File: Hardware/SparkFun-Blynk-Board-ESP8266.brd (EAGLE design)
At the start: 50 x 41.9 mm, 104 parts, among them IC1 LMV358, Q1 2.5A/30V, Q2 MMBT2222A, Q3 MMBT2222A, U1 MCP73831, U2 ESP8266, U3 AP2112K-3.3V, U4 FT231XS-U, U5 W25Q32FVSS, U6 SI7021, Y1 26MHz

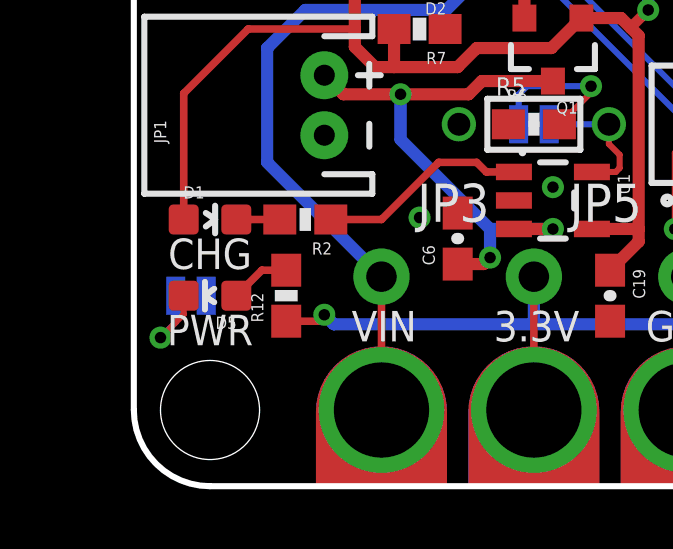
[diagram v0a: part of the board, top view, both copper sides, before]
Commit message: Moving PWR led a bit away from screwhead.
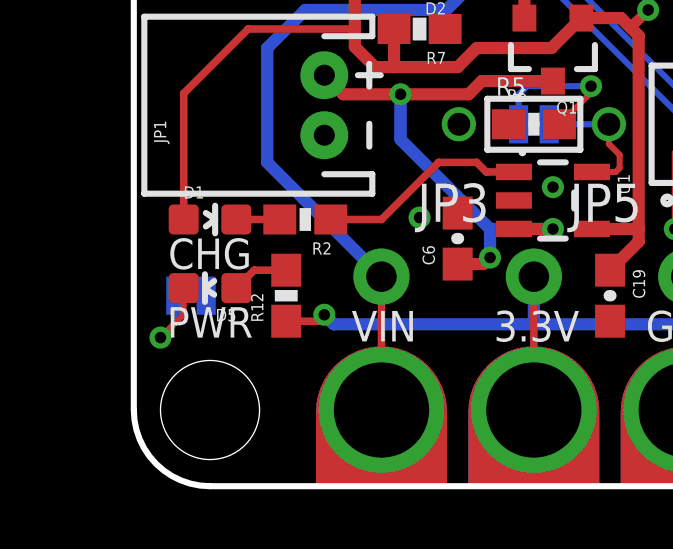
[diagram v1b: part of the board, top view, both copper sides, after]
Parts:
- moved D5 0.25 mm to (2.54, 6.60)
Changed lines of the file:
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@@
 <board>
 <plain>
-<text x="2.54" y="5.715" size="1.016" layer="21" font="vector" ratio="15" rot="R180" align="bottom-center">PWR</text>
+<text x="2.54" y="5.969" size="1.016" layer="21" font="vector" ratio="15" rot="R180" align="bottom-center">PWR</text>
 <wire x1="0" y1="2.54" x2="0" y2="39.37" width="0.2032" layer="20"/>
 <wire x1="0" y1="39.37" x2="2.54" y2="41.91" width="0.2032" layer="20" curve="-90"/>
@@
 <attribute name="PROD_ID" value="RES-07856" x="6.35" y="-36.83" size="1.778" layer="27" font="vector" ratio="15" rot="R90" display="off"/>
 </element>
-<element name="D5" library="SparkFun-LED" package="LED-0603" value="RED" x="2.54" y="6.35" rot="R90">
-<attribute name="PROD_ID" value="DIO-00819" x="8.89" y="-34.29" size="1.778" layer="27" font="vector" ratio="15" rot="R90" display="off"/>
+<element name="D5" library="SparkFun-LED" package="LED-0603" value="RED" x="2.54" y="6.604" rot="R90">
+<attribute name="PROD_ID" value="DIO-00819" x="8.89" y="-34.036" size="1.778" layer="27" font="vector" ratio="15" rot="R90" display="off"/>
 </element>
 <element name="R6" library="SparkFun-Resistors" package="0603-RES" value="2.0k" x="13.335" y="12.065">
@@
 <contactref element="D5" pad="C"/>
 <contactref element="SJ2" pad="2"/>
-<wire x1="1.663" y1="6.35" x2="1.663" y2="5.727" width="0.2032" layer="1"/>
+<wire x1="1.663" y1="6.604" x2="1.663" y2="5.727" width="0.2032" layer="1"/>
 <wire x1="1.663" y1="5.727" x2="0.889" y2="4.953" width="0.2032" layer="1"/>
 <via x="0.889" y="4.953" extent="1-16" drill="0.381"/>
@@
 <contactref element="D5" pad="A"/>
 <contactref element="R12" pad="2"/>
-<wire x1="3.417" y1="6.35" x2="4.267" y2="7.2" width="0.254" layer="1"/>
-<wire x1="4.267" y1="7.2" x2="5.08" y2="7.2" width="0.254" layer="1"/>
+<wire x1="3.417" y1="6.604" x2="4.013" y2="7.2" width="0.254" layer="1"/>
+<wire x1="4.013" y1="7.2" x2="5.08" y2="7.2" width="0.254" layer="1"/>
 </signal>
 <signal name="N$11">

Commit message: Adding values to all parts
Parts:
- JP1: value LiPo -> JST-2
- JP10, JP11, JP12, JP13, JP16, JP17, JP18, JP19, JP2, JP20, JP21, JP22, JP23, JP24, JP25, JP26, JP27, JP28, JP3, JP30, JP4, JP5, JP6, JP7, JP8, JP9, SJ1, SJ4: value (none) -> DNP
- JP14: value (none) -> JST-3
- JP15: value (none) -> USB
- JP29: value (none) -> JST-4
- S1: value (none) -> GP0

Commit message: Adding value to 2-pin JST
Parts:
- JP1: value JST-2 -> JST_2
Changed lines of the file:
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@@
 <attribute name="PROD_ID" value="RES-00824" x="32.385" y="5.08" size="1.778" layer="27" font="vector" ratio="15" rot="R180" display="off"/>
 </element>
-<element name="JP1" library="SparkFun-Connectors" package="JST-2-PTH" value="JST-2" x="6.35" y="12.7" rot="R90">
+<element name="JP1" library="SparkFun-Connectors" package="JST-2-PTH" value="JST_2" x="6.35" y="12.7" rot="R90">
 <attribute name="SKU" value="PRT-09914" x="7.62" y="-5.08" size="1.778" layer="27" font="vector" ratio="15" rot="R90" display="off"/>
 <attribute name="PROD_ID" value="CONN-09863" x="7.62" y="-5.08" size="1.778" layer="27" font="vector" ratio="15" rot="R90" display="off"/>
